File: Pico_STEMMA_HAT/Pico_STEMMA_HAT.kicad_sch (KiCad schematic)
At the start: 39 parts, among them J1 Conn_01x20_Socket, J2 Conn_01x20_Socket, J3 SDCARD_MODULE

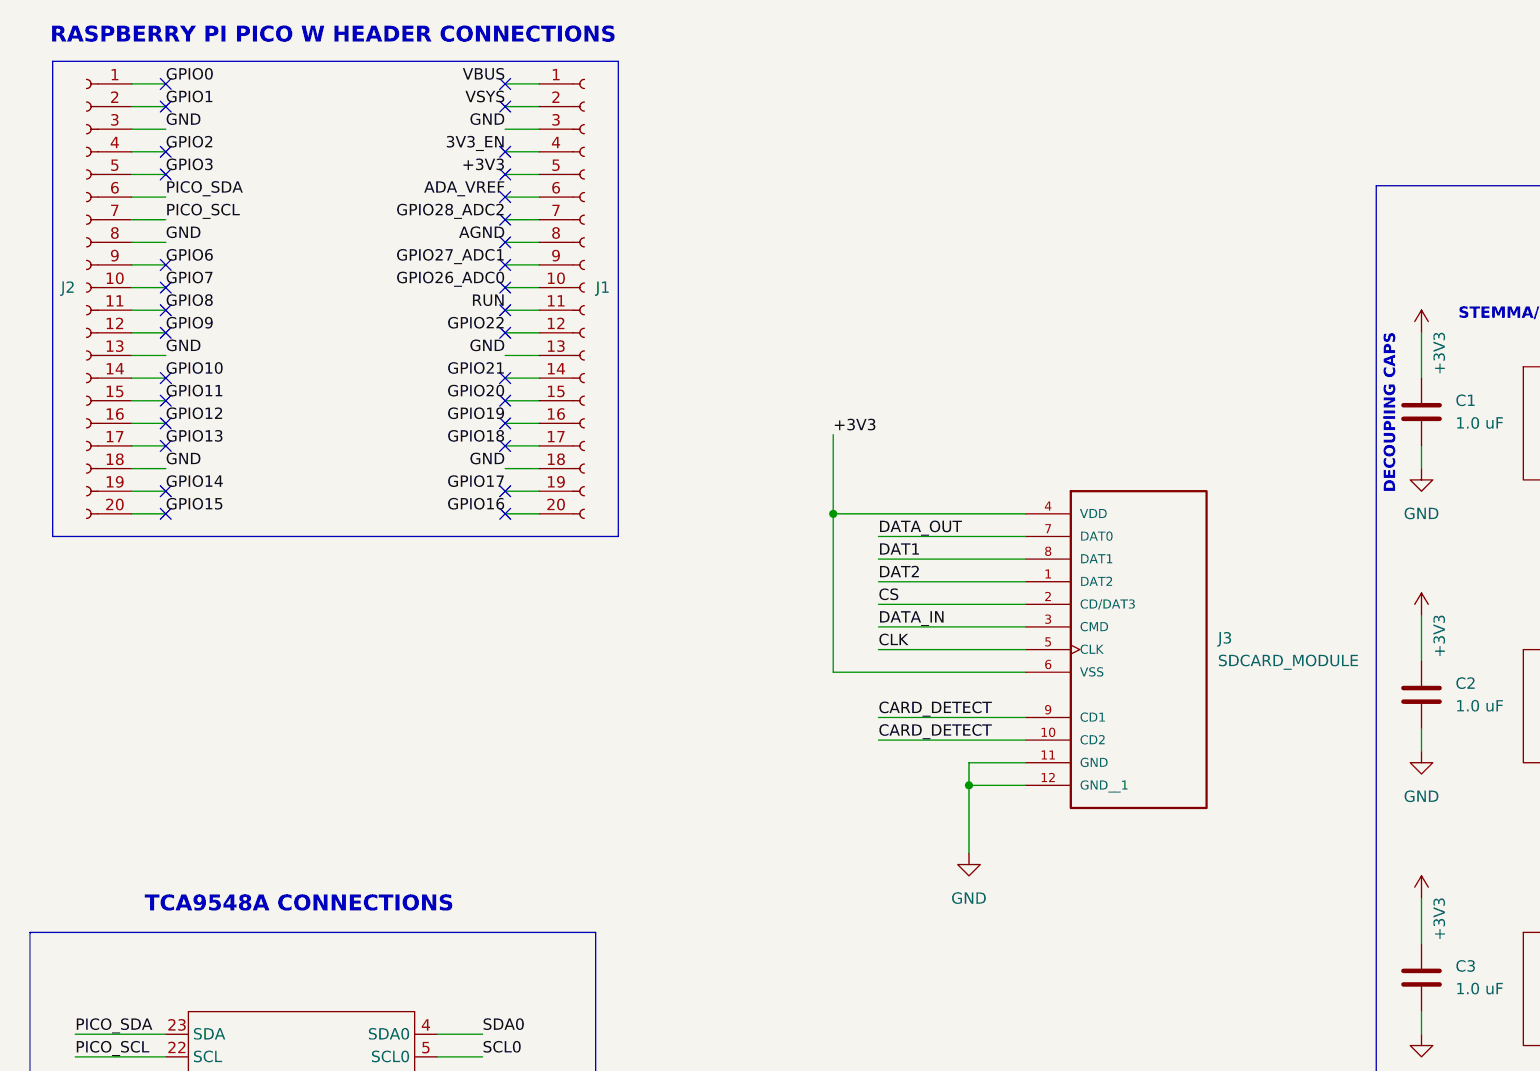
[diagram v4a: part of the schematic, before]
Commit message: Add SD card reader to PCB design
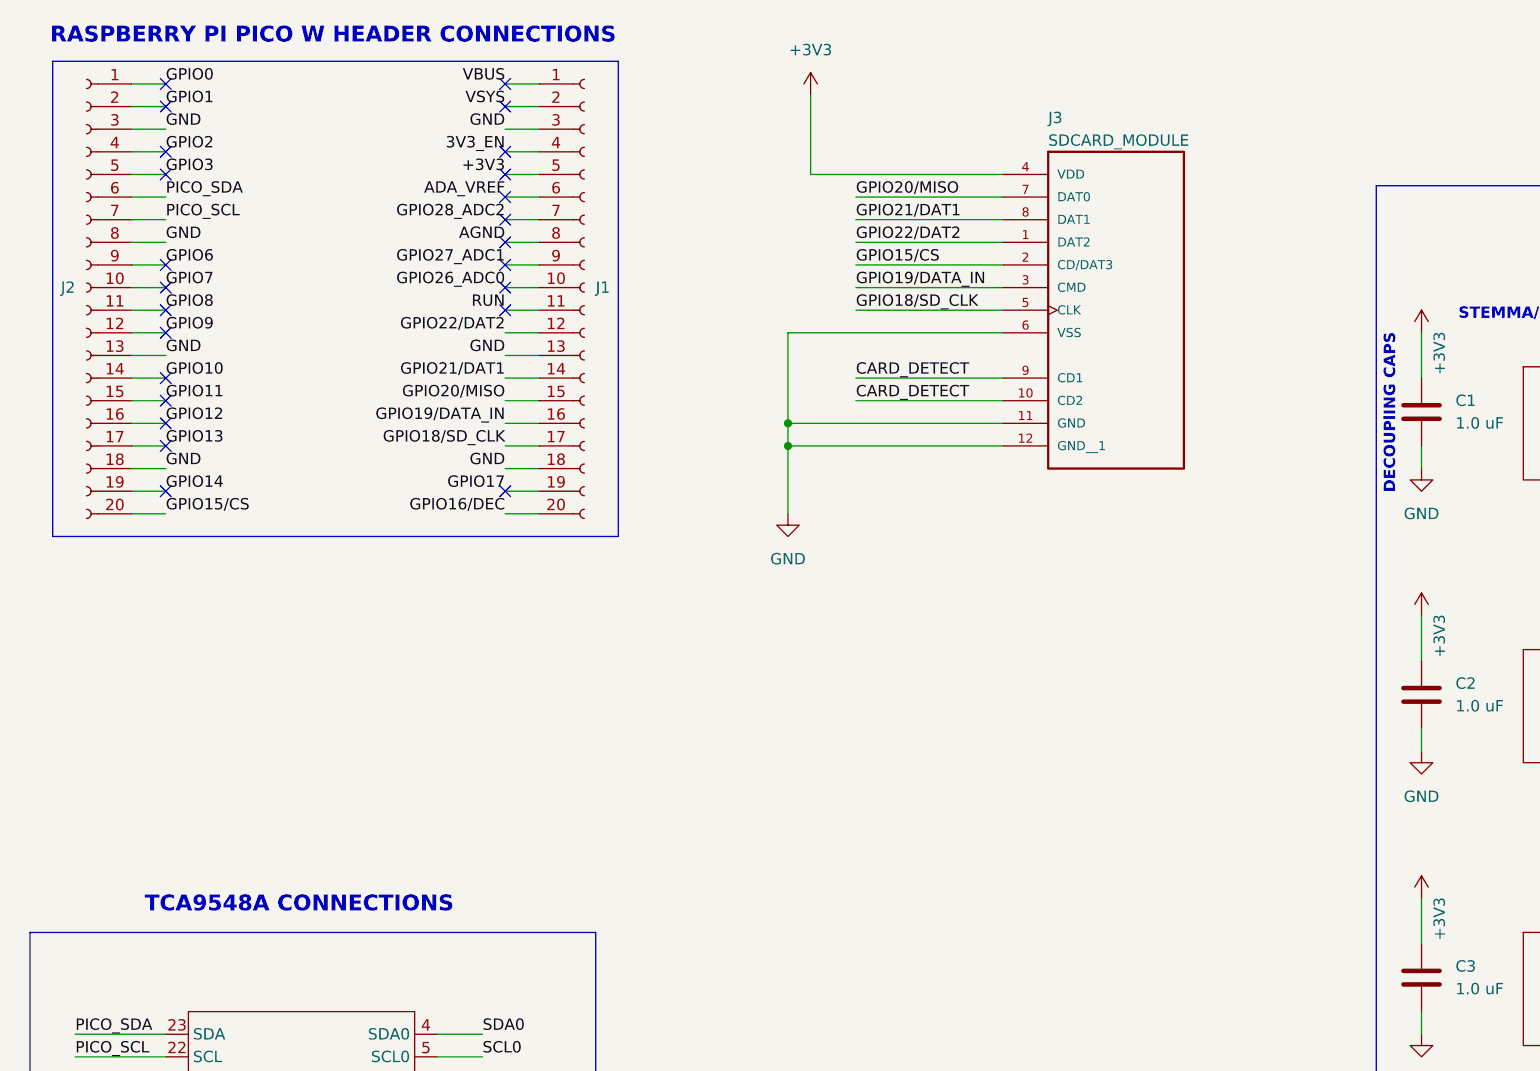
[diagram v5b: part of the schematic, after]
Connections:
- net GPIO15 is gone; now on net GPIO15/CS: J2.20 (Pin_20)
- net GPIO18 is gone; now on net GPIO18/SD_CLK: J1.17 (Pin_17)
- net GPIO19 is gone; now on net GPIO19/DATA_IN: J1.16 (Pin_16)
- net GPIO20 is gone; now on net GPIO20/MISO: J1.15 (Pin_15)
- net GPIO21 is gone; now on net GPIO21/DAT1: J1.14 (Pin_14)
- net GPIO22 is gone; now on net GPIO22/DAT2: J1.12 (Pin_12)
- net +3V3: no longer J3.6 (VSS)
- net GND: now also J3.6 (VSS)
- net CLK renamed GPIO18/SD_CLK
- net CS renamed GPIO15/CS
- net DAT1 renamed GPIO21/DAT1
- net DAT2 renamed GPIO22/DAT2
- net DATA_IN renamed GPIO19/DATA_IN
- net DATA_OUT renamed GPIO20/MISO
- net GPIO16 renamed GPIO16/DEC
- no-connect marks 35 -> 28
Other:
- moved on the sheet: J3

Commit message: Add pullup resistors to the SD card reader
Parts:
- added R18, R19: 47k, Resistor_SMD:R_0603_1608Metric, symbol Device:R_US
- added RN1: 47k, Resistor_SMD:R_Array_Concave_4x0402, symbol Device:R_Pack04
- added U1: Neopixel, Pico_Footprints:NEOPIXEL_Footprint, symbol Pico_Symbols:NEOPIXEL
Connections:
- net +3V3: now also R18.2, R19.2, RN1.5 (R4.2), RN1.6 (R3.2), RN1.7 (R2.2), RN1.8 (R1.2), U1.2 (VDD)
- net GND: now also U1.4 (GND)
- net GPIO15/CS: now also RN1.4 (R4.1)
- net GPIO18/SD_CLK: now also R19.1
- net GPIO19/DATA_IN: now also R18.1
- net GPIO20/MISO: now also RN1.2 (R2.1)
- net GPIO21/DAT1: now also RN1.1 (R1.1)
- net GPIO22/DAT2: now also RN1.3 (R3.1)
- net GPIO6 renamed GPIO6/NEOPIXEL
- net GPIO6/NEOPIXEL: now also U1.1 (DIN)
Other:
- moved on the sheet: C1, C2, C3, C4, C5, C6, C7, C8, J3, R1, R10, R11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

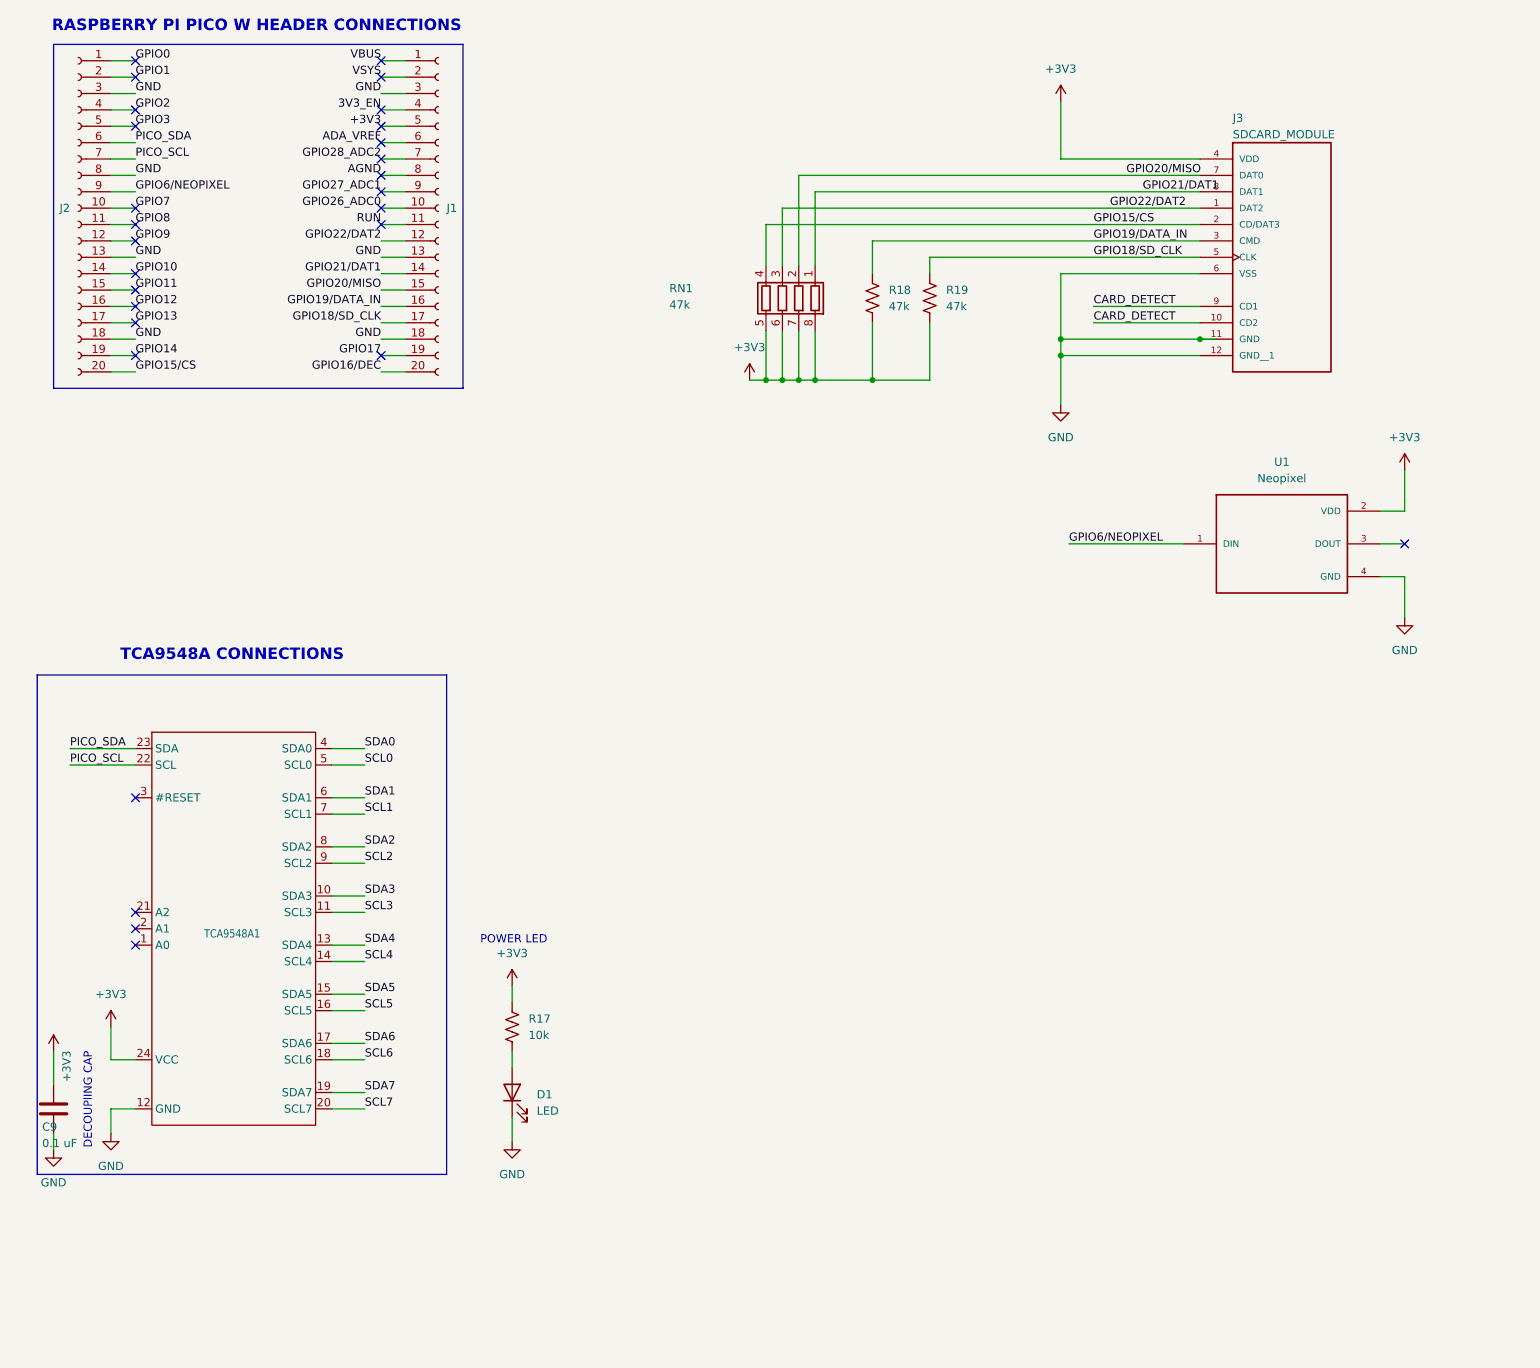
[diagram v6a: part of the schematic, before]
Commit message: Change pullup resistors
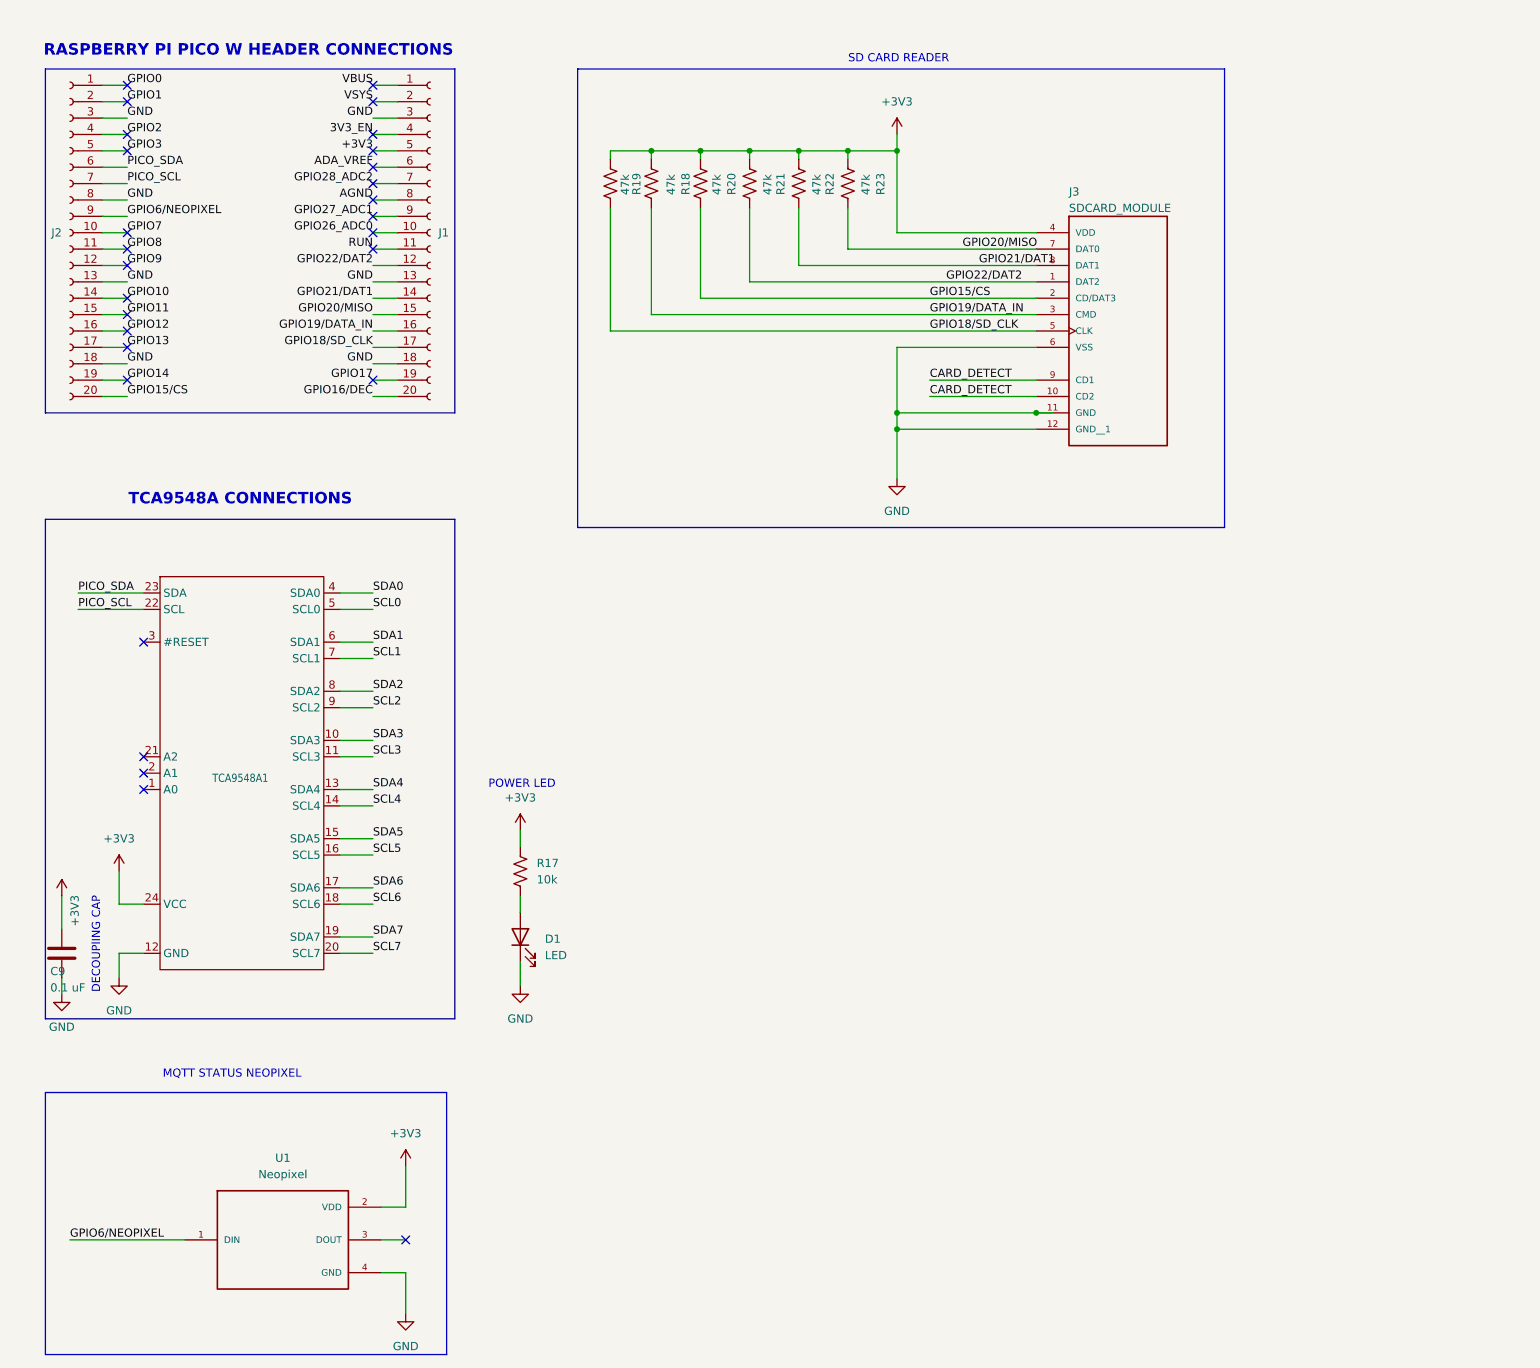
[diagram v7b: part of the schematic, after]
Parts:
- removed RN1: 47k, Resistor_SMD:R_Array_Concave_4x0402, symbol Device:R_Pack04
- added R20, R21, R22, R23: 47k, Resistor_SMD:R_0603_1608Metric, symbol Device:R_US
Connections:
- net +3V3: now also R18.1, R19.1, R20.1, R21.1, R22.1, R23.1; no longer R18.2, R19.2
- net GPIO15/CS: now also R20.2
- net GPIO18/SD_CLK: now also R19.2; no longer R19.1
- net GPIO19/DATA_IN: now also R18.2; no longer R18.1
- net GPIO20/MISO: now also R23.2
- net GPIO21/DAT1: now also R22.2
- net GPIO22/DAT2: now also R21.2
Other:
- note added: "MQTT STATUS NEOPIXEL"
- note added: "SD CARD READER"
- moved on the sheet: C9, D1, J1, J2, J3, R17, R18, R19, TCA9548A1, U1
